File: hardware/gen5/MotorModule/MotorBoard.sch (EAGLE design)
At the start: 53 parts, among them IC2 3.3V REG, M1O1 TEST_PT, M1O2 TEST_PT, M1O3 TEST_PT

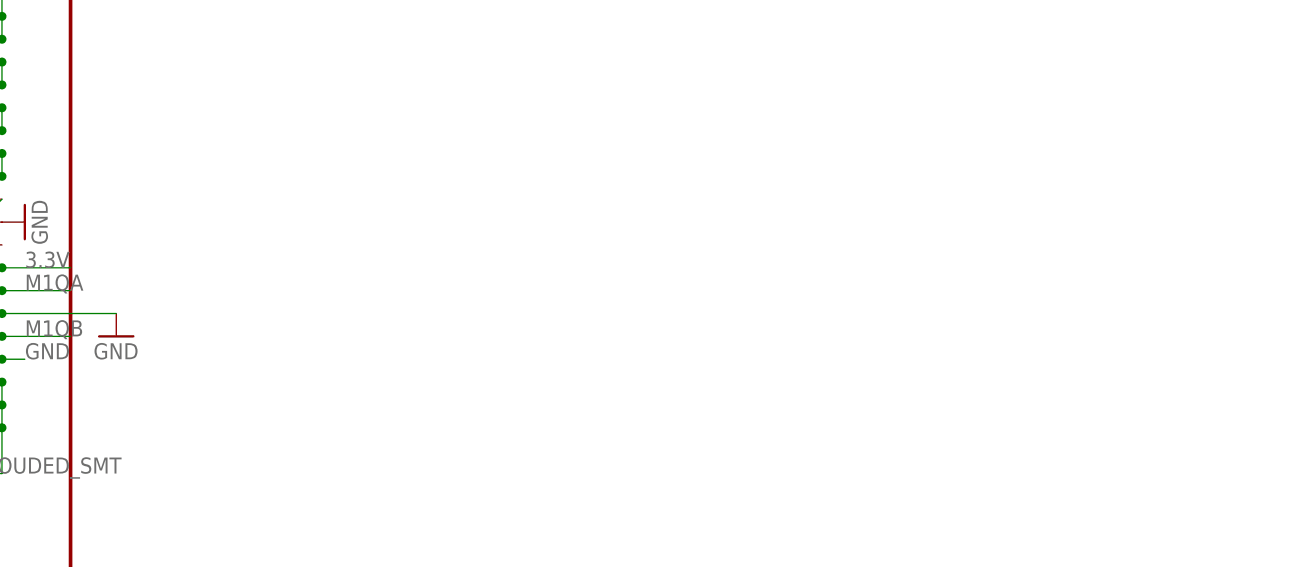
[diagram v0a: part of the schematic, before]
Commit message: finished control module - needs review - might need more condensing?
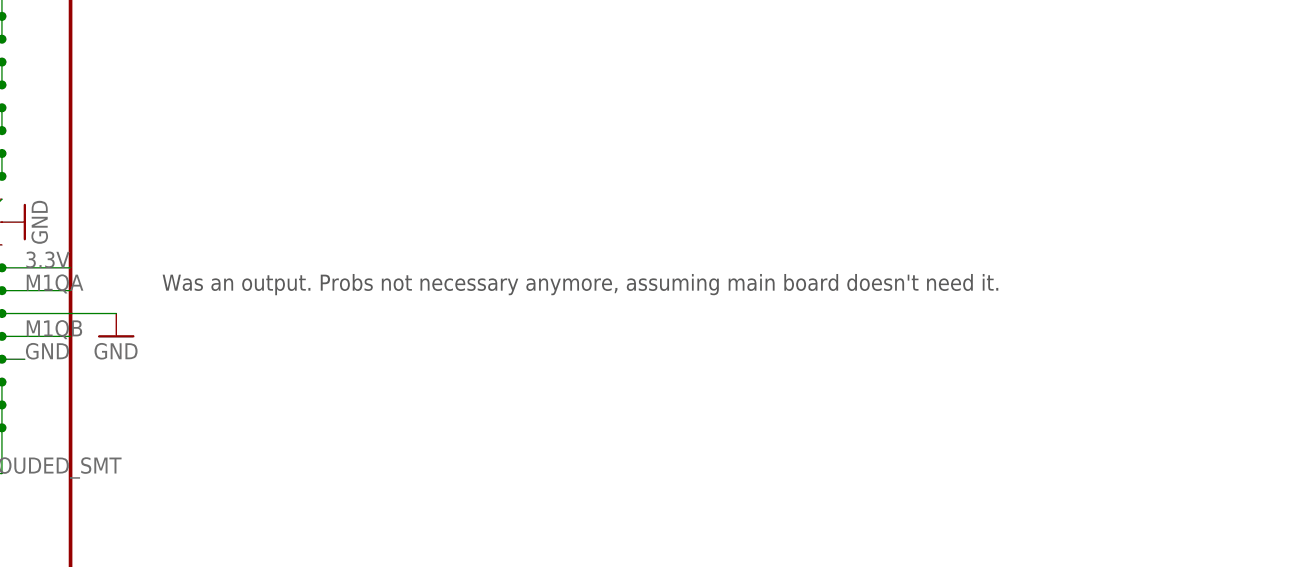
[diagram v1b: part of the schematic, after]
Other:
- note added: "Was an output. Probs not necessary anymore, assuming main board doesn't need it."
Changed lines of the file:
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@@
 <?xml version="1.0" encoding="utf-8"?>
 <!DOCTYPE eagle SYSTEM "eagle.dtd">
-<eagle version="7.4.0">
+<eagle version="7.2.0">
 <drawing>
 <settings>
@@
 to our main MCU</text>
 <text x="254" y="43.18" size="1.778" layer="99">Why do we have a 3.3V input here?</text>
+<text x="259.08" y="40.64" size="1.778" layer="97">Was an output. Probs not necessary anymore, assuming main board doesn't need it.</text>
 </plain>
 <instances>

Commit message: finished motor board schematic and rudimentary placement - needs discussion
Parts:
- removed JP3: M20X2SHROUDED_SMT, SparkFun-Connectors:M20X2SHROUDED_SMT
- removed R105, R106, R107: 4.7k, SparkFun-Resistors:RESISTOR0805-RES
- removed R11, R78, R79: 1k, SparkFun-Resistors:RESISTOR0805-RES
- added R2, R3, R4: 4.7k, SparkFun-Resistors:RESISTOR0805-RES
- added SV1, SV2: (no value), con-lstb:MA10-1W
- R63, R7: value 30k -> 1k
- R9: value 15k -> 1k
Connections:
- removed net BREN: JP3.27, R79.2
- removed net M1QA: JP3.28
- removed net M1QB: JP3.32
- removed net N$23: R79.1, U$1.BRAKE
- removed net N$28: R63.2, U$1.FAULTN
- removed net N$3: R11.1, U$1.ENABLEN
- removed net N$31: R9.2, U$1.HALLOUT
- removed net N$4 (its old number): R7.2, U$1.LOCKN
- removed net N$98: R78.1, U$1.DIR
- removed net PWM1: JP3.29, U$1.PWM
- removed net TSENSE1: JP3.31, U$5.VO
- new net BRAKE: R103.2, SV2.6, U$1.BRAKE
- new net FAULTN: LED11.C, R63.2, SV2.2, U$1.FAULTN
- new net HALLOUT: R9.2, SV2.3, U$1.HALLOUT
- new net LOCKN: LED13.C, R7.2, SV2.1, U$1.LOCKN
- new net PWM: SV2.5, U$1.PWM
- new net TSENSE: U$5.VO
- net 12V: now also SV1.10, SV1.6, SV1.7, SV1.8, SV1.9; no longer JP3.1, JP3.2, JP3.3, JP3.4, JP3.5, JP3.6
- net 12VGND: now also SV1.1, SV1.2, SV1.3, SV1.4, SV1.5; no longer JP3.35, JP3.36, JP3.37, JP3.38, JP3.39, JP3.40
- net 3.3V: now also R101.2, R99.2; no longer JP3.26
- net 5V: now also R2.1, R3.1, R4.1; no longer JP3.23, R105.2, R106.2, R107.2
- net DIR: now also SV2.7, U$1.DIR; no longer JP3.25, R78.2
- net ENABLE: now also R1.2, SV2.4, U$1.ENABLEN; no longer R11.2
- net GND: no longer JP3.22, JP3.30, JP3.33, JP3.34, LED11.C, LED13.C
- net M1H1: now also R2.2, SV2.9; no longer JP3.19, R106.1
- net M1H2: now also R3.2, SV2.10; no longer JP3.20, R107.1
- net M1H3: now also R4.2, SV2.8; no longer JP3.21, R105.1
- net M1O1: no longer JP3.11, JP3.12, JP3.13, JP3.14
- net M1O2: no longer JP3.10, JP3.7, JP3.8, JP3.9
- net M1O3: no longer JP3.15, JP3.16, JP3.17, JP3.18
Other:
- note added: "Do we need this?"
- note added: "Might need more than this"
- note added: "Need to connect these with high current"
- note added: "Separate connector?"
- note removed: "Was an output. Probs not necessary anymore, assuming main board doesn't need it."
- note removed: "We may want to make these fault signals inputs to our main MCU"
- note removed: "Why do we have a 3.3V input here?"
- moved on the sheet: C1, C12, C13, C2, C3, C4, C5, C6, C7, C8, D5, IC2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

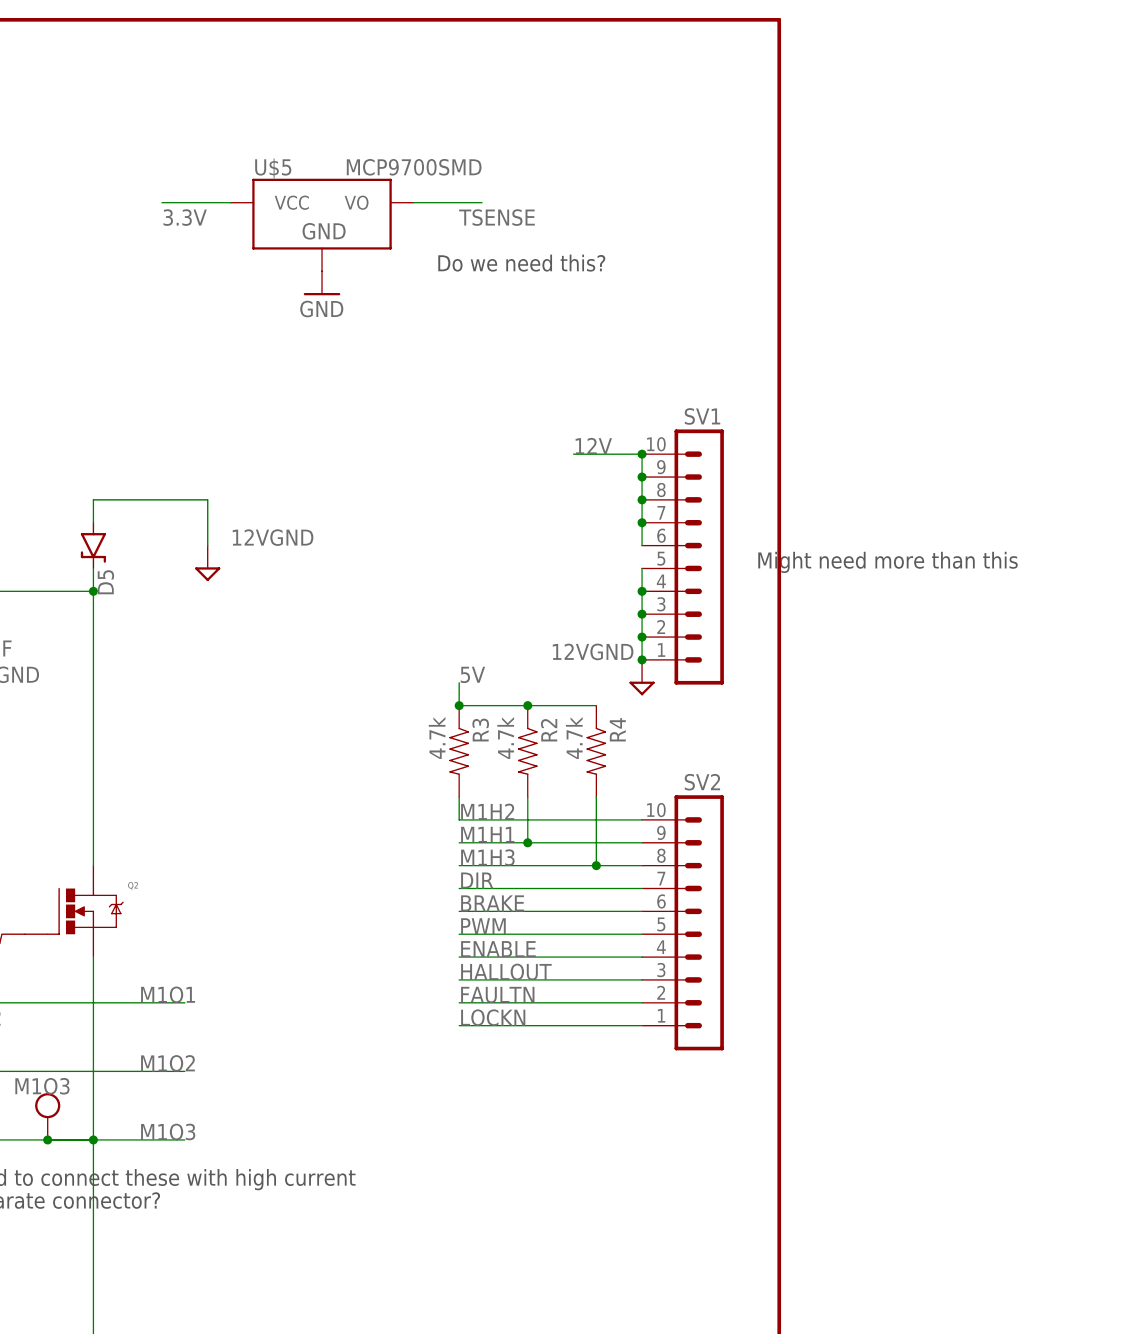
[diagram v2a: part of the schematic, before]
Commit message: Working on motor board layout - should be done soon
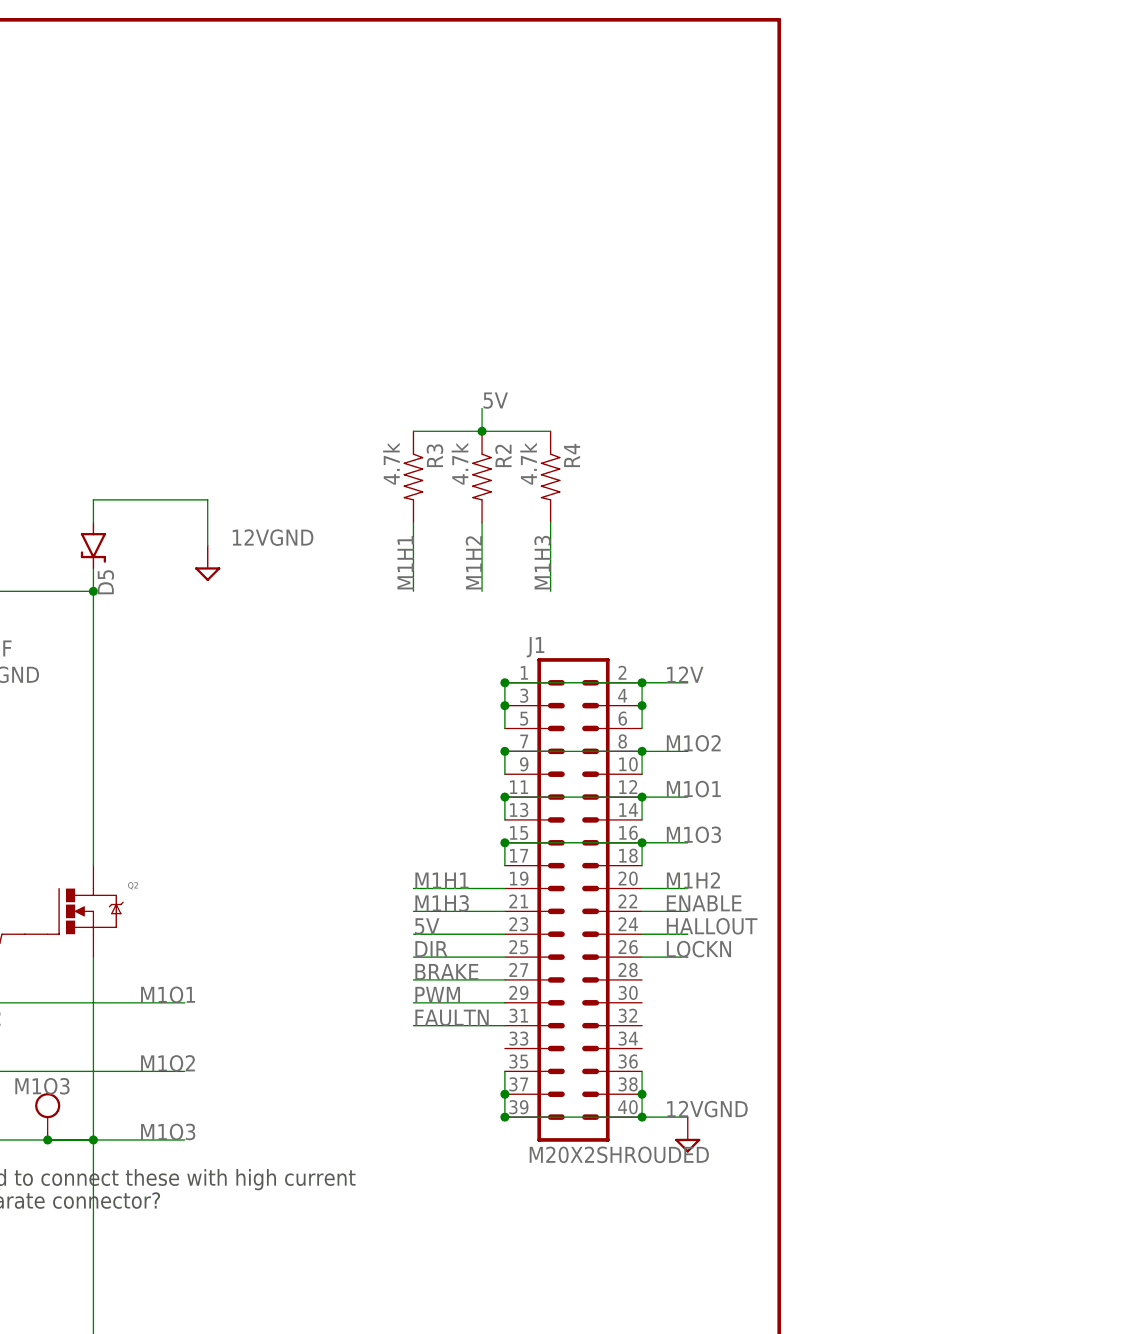
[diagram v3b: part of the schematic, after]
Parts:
- removed SV1, SV2: (no value), con-lstb:MA10-1W
- removed U$5: MCP9700SMD, SparkFun-Sensors:MCP9700SMD
- added J1: M20X2SHROUDED, SparkFun-Connectors:M20X2SHROUDED
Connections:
- removed net TSENSE: U$5.VO
- net 12V: now also J1.1, J1.2, J1.3, J1.4, J1.5, J1.6; no longer SV1.10, SV1.6, SV1.7, SV1.8, SV1.9
- net 12VGND: now also J1.35, J1.36, J1.37, J1.38, J1.39, J1.40; no longer SV1.1, SV1.2, SV1.3, SV1.4, SV1.5
- net 3.3V: no longer U$5.VCC
- net 5V: now also J1.23
- net BRAKE: now also J1.27; no longer SV2.6
- net DIR: now also J1.25; no longer SV2.7
- net ENABLE: now also J1.22; no longer SV2.4
- net FAULTN: now also J1.31; no longer SV2.2
- net GND: no longer U$5.GND
- net HALLOUT: now also J1.24; no longer SV2.3
- net LOCKN: now also J1.26; no longer SV2.1
- net M1H1: now also J1.19, R3.2; no longer R2.2, SV2.9
- net M1H2: now also J1.20, R2.2; no longer R3.2, SV2.10
- net M1H3: now also J1.21; no longer SV2.8
- net M1O1: now also J1.11, J1.12, J1.13, J1.14
- net M1O2: now also J1.10, J1.7, J1.8, J1.9
- net M1O3: now also J1.15, J1.16, J1.17, J1.18
- net PWM: now also J1.29; no longer SV2.5
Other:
- note removed: "Do we need this?"
- note removed: "Might need more than this"
- moved on the sheet: R2, R3, R4

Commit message: Motor board finished - needs review
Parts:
- removed M1O1, M1O2, M1O3: TEST_PT, gen3:TEST_PT
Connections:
- net 12VGND: now also J1.22, J1.33, J1.34
- net ENABLE: now also J1.30; no longer J1.22
- net M1O1: no longer M1O1.P$1
- net M1O2: no longer M1O2.P$1
- net M1O3: no longer M1O3.P$1
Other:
- note added: "24, 26, and 30 are unconnected in Rev A"
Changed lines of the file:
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@@
 <part name="C7" library="gen3" deviceset="CAP-POLAR" device="" value="100uF"/>
 <part name="D5" library="gen3" deviceset="DIODE-ZENER" device="DO214AC" value="DIODE-ZENERDO214AC"/>
-<part name="M1O1" library="gen3" deviceset="TEST_PT" device=""/>
-<part name="M1O2" library="gen3" deviceset="TEST_PT" device=""/>
-<part name="M1O3" library="gen3" deviceset="TEST_PT" device=""/>
 <part name="C2" library="gen3" deviceset="CAP-POLAR" device="" value="100uF"/>
 <part name="GEN_5_REV_A" library="gen3" deviceset="LOGO" device="" value="Fall 2016"/>
@@
 <text x="157.48" y="55.88" size="1.778" layer="97">Need to connect these with high current</text>
 <text x="157.48" y="53.34" size="1.778" layer="97">Separate connector?</text>
+<text x="254" y="81.28" size="1.778" layer="97">24, 26, and 30 are unconnected in Rev A</text>
 </plain>
 <instances>
@@
 <instance part="C7" gate="G$1" x="137.16" y="119.38"/>
 <instance part="D5" gate="G$1" x="172.72" y="127" rot="R270"/>
-<instance part="M1O1" gate="G$1" x="139.7" y="78.74"/>
-<instance part="M1O2" gate="G$1" x="160.02" y="71.12"/>
-<instance part="M1O3" gate="G$1" x="167.64" y="63.5"/>
 <instance part="C2" gate="G$1" x="144.78" y="119.38"/>
 <instance part="GEN_5_REV_A" gate="G$1" x="7.62" y="22.86"/>
@@
 <label x="236.22" y="63.5" size="1.778" layer="95"/>
 <pinref part="12VGND4" gate="GND" pin="GND"/>
+<pinref part="J1" gate="G$1" pin="33"/>
+<wire x1="218.44" y1="68.58" x2="218.44" y2="71.12" width="0.1524" layer="91"/>
+<junction x="218.44" y="68.58"/>
+<pinref part="J1" gate="G$1" pin="34"/>
+<wire x1="233.68" y1="68.58" x2="233.68" y2="71.12" width="0.1524" layer="91"/>
+<junction x="233.68" y="68.58"/>
+</segment>
+<segment>
+<pinref part="J1" gate="G$1" pin="22"/>
+<wire x1="233.68" y1="86.36" x2="238.76" y2="86.36" width="0.1524" layer="91"/>
+<label x="236.22" y="86.36" size="1.778" layer="95"/>
 </segment>
 </net>
@@
 <pinref part="Q6" gate="G$1" pin="P$2"/>
 <wire x1="104.14" y1="76.2" x2="132.08" y2="76.2" width="0.1524" layer="91"/>
-<wire x1="139.7" y1="76.2" x2="132.08" y2="76.2" width="0.1524" layer="91"/>
 <junction x="132.08" y="76.2"/>
 <pinref part="Q3" gate="G$1" pin="P$1"/>
 <wire x1="132.08" y1="76.2" x2="132.08" y2="58.42" width="0.1524" layer="91"/>
 <wire x1="132.08" y1="99.06" x2="132.08" y2="76.2" width="0.1524" layer="91"/>
-<pinref part="M1O1" gate="G$1" pin="P$1"/>
 <pinref part="U$1" gate="G$1" pin="W"/>
-<wire x1="139.7" y1="76.2" x2="182.88" y2="76.2" width="0.1524" layer="91"/>
-<junction x="139.7" y="76.2"/>
+<wire x1="132.08" y1="76.2" x2="182.88" y2="76.2" width="0.1524" layer="91"/>
 <label x="177.8" y="76.2" size="1.778" layer="95"/>
 </segment>
@@
 <wire x1="152.4" y1="68.58" x2="152.4" y2="43.18" width="0.1524" layer="91"/>
 <pinref part="Q4" gate="G$1" pin="P$1"/>
-<pinref part="M1O2" gate="G$1" pin="P$1"/>
 <wire x1="104.14" y1="68.58" x2="160.02" y2="68.58" width="0.1524" layer="91"/>
 <pinref part="U$1" gate="G$1" pin="V"/>
@@
 <wire x1="172.72" y1="81.28" x2="172.72" y2="60.96" width="0.1524" layer="91"/>
 <wire x1="172.72" y1="60.96" x2="172.72" y2="33.02" width="0.1524" layer="91"/>
-<pinref part="M1O3" gate="G$1" pin="P$1"/>
-<junction x="167.64" y="60.96"/>
 <pinref part="U$1" gate="G$1" pin="U"/>
 <wire x1="172.72" y1="60.96" x2="182.88" y2="60.96" width="0.1524" layer="91"/>
@@
 </segment>
 <segment>
-<pinref part="J1" gate="G$1" pin="22"/>
-<wire x1="233.68" y1="86.36" x2="238.76" y2="86.36" width="0.1524" layer="91"/>
-<label x="236.22" y="86.36" size="1.778" layer="95"/>
-</segment>
-</net>
+<pinref part="J1" gate="G$1" pin="30"/>
+<wire x1="233.68" y1="76.2" x2="238.76" y2="76.2" width="0.1524" layer="91"/>
+<label x="236.22" y="76.2" size="1.778" layer="95"/>
+</segment>
+</net>
